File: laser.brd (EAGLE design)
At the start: 7 parts

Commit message: Test layout
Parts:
- removed E$2: (no value), EasyDriver:EASYDRIVER_V44
- added DC_JACK: (no value), SparkFun-Connectors:POWER_JACK_SLOT
- added E$7: (no value), SparkFun-DiscreteSemi:TO-92
- added E$8: (no value), SparkFun-DiscreteSemi:DIODE-1N4001
- added E$9: (no value), eagle-ltspice:0204/7
- added END_X1, END_Y1, FAN, FAN1, LASER: (no value), pinhead:1X02
- added LM317: (no value), v-reg:78XXL
- added X_AXIS, Y_AXIS: (no value), EasyDriver:EASYDRIVER_V44
- added X_AXIS_CON, Y_AXIS_CON: (no value), SparkFun-Connectors:1X04_LONGPADS
- E$1: device v-reg:78XXL -> heatsink:D01S
- E$3: device EasyDriver:EASYDRIVER_V44 -> jumper:0R/10E
- E$5: device SparkFun-Resistors:AXIAL-0.6 -> jumper:07
- NANO: value (none) -> NANO
- moved E$3 76.0 mm to (-6.35, 71.1), turned to 180 degrees
- moved E$1 62.2 mm to (69.8, 52.1)
- moved E$5 48.7 mm to (-6.35, 68.6), turned to 180 degrees
- moved NANO 45.8 mm to (33.0, 74.9)
- moved E$4 44.3 mm to (62.2, 35.6), turned to 180 degrees
- moved E$6 19.1 mm to (66.0, 72.4), turned to 180 degrees
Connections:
- new net 12V: DC_JACK.PWR, E$8.A, FAN.2, FAN1.2, X_AXIS.M+, Y_AXIS.M+
- new net 5V: NANO.D9, X_AXIS.MS1, X_AXIS.MS2, X_AXIS.P$11, Y_AXIS.MS1, Y_AXIS.MS2, Y_AXIS.P$11
- new net GND: DC_JACK.GND@1, DC_JACK.GND@2, E$7.3, END_X1.2, END_Y1.2, FAN.1, FAN1.1, NANO.A7, NANO.D11, X_AXIS.GND1, X_AXIS.GND2, X_AXIS.GND3, Y_AXIS.GND1, Y_AXIS.GND2, Y_AXIS.GND3
- new net S$1: NANO.A6, Y_AXIS.STEP
- new net S$10: X_AXIS.B1, X_AXIS_CON.1
- new net S$11: Y_AXIS.B1, Y_AXIS_CON.1
- new net S$12: Y_AXIS.B2, Y_AXIS_CON.2
- new net S$13: Y_AXIS.A2, Y_AXIS_CON.3
- new net S$14: Y_AXIS.A1, Y_AXIS_CON.4
- new net S$15: E$8.C, LM317.IN
- new net S$16: E$4.P$2, LM317.OUT
- new net S$17: E$4.P$1, E$6.A, E$6.S
- new net S$18: E$6.E, LASER.2, LM317.GND
- new net S$19: E$9.1, NANO.VIN
- new net S$2: NANO.A5, X_AXIS.STEP
- new net S$20: E$7.2, E$9.2
- new net S$21: E$7.1, LASER.1
- new net S$3: NANO.A3, Y_AXIS.DIR
- new net S$4: NANO.A2, X_AXIS.DIR
- new net S$7: X_AXIS.A1, X_AXIS_CON.4
- new net S$8: X_AXIS.A2, X_AXIS_CON.3
- new net S$9: X_AXIS.B2, X_AXIS_CON.2
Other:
- board outline added: 7.1 x 7.3 mm

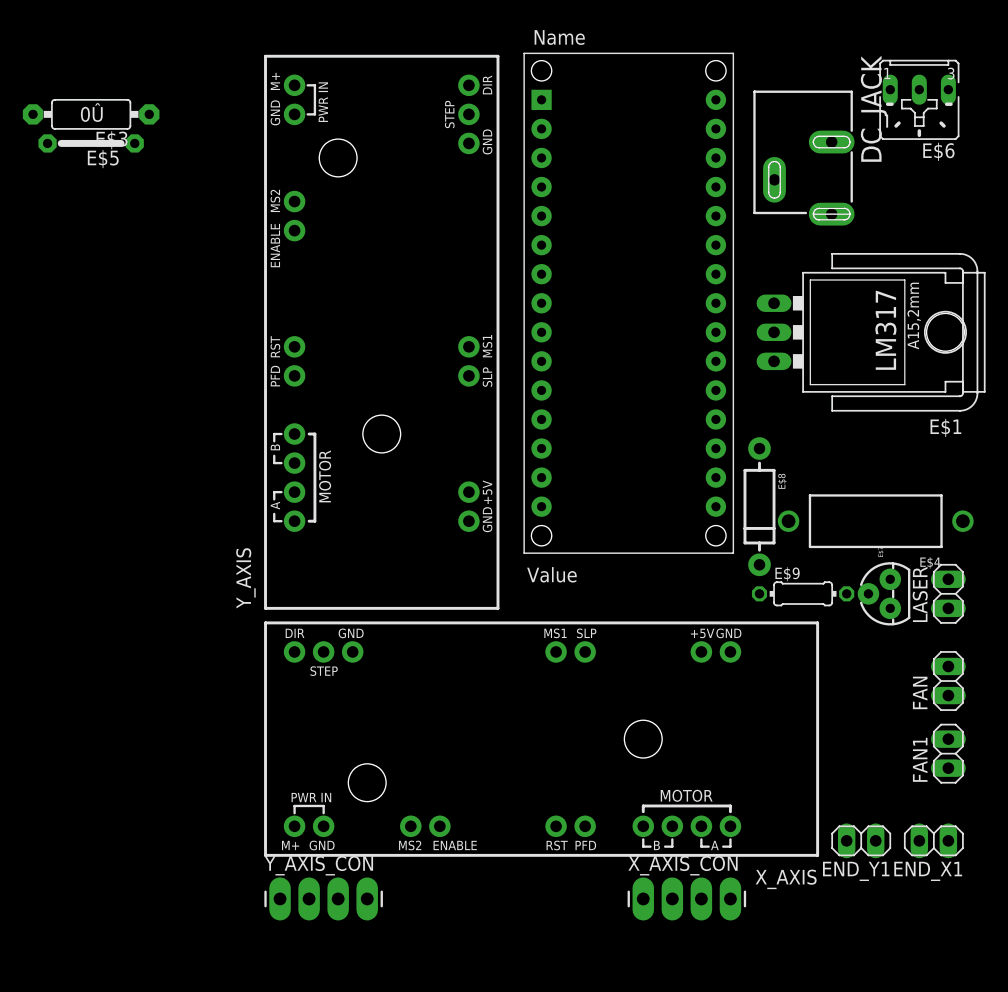
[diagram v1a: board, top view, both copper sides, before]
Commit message: Test layout, added power switch
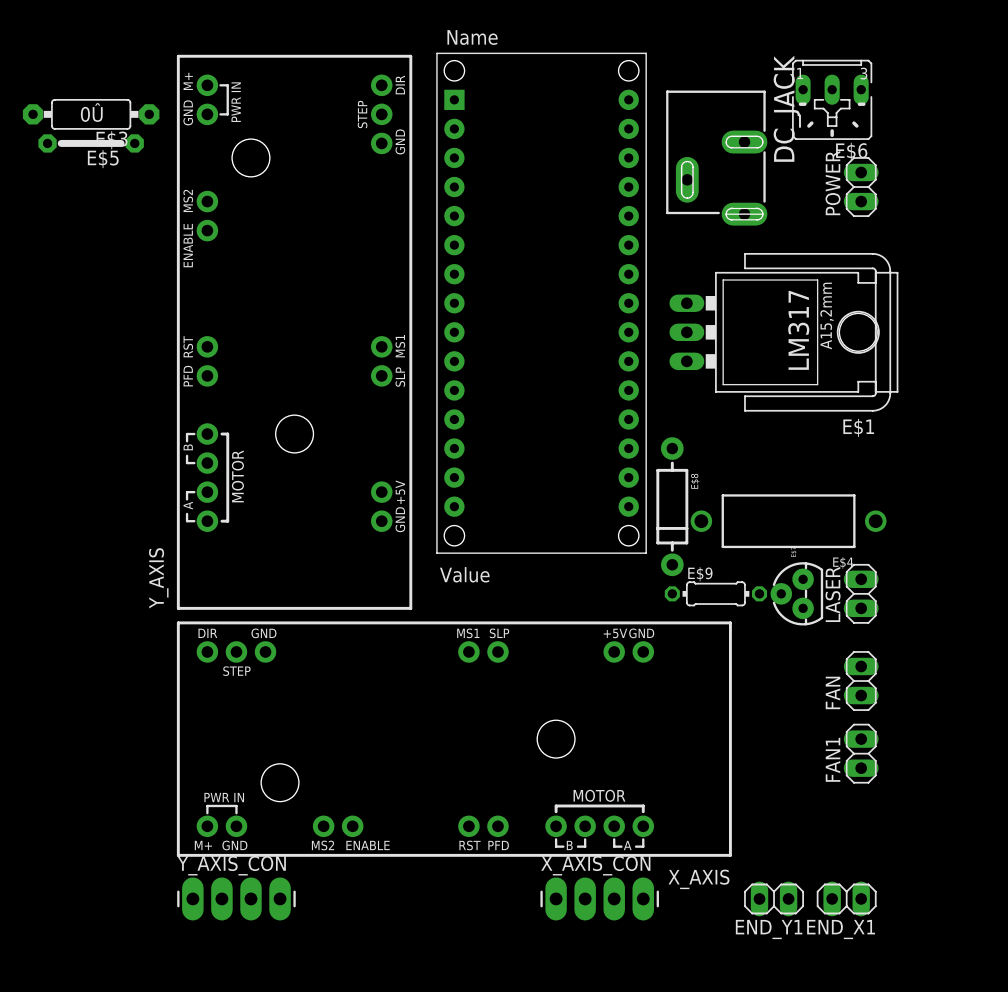
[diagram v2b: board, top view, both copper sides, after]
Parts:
- added POWER: (no value), pinhead:1X02
- moved END_X1 9.16 mm to (59.7, 2.54)
- moved END_Y1 9.16 mm to (53.3, 2.54)
- moved E$6 7.62 mm to (58.4, 72.4)
- moved E$9 7.62 mm to (48.3, 29.2)
- moved NANO 7.62 mm to (25.4, 74.9)
- moved X_AXIS 7.62 mm to (25.4, 16.5)
- moved Y_AXIS 7.62 mm to (11.4, 52.1)
- moved Y_AXIS_CON 7.62 mm to (2.54, 2.54)
- moved DC_JACK 7.62 mm to (53.3, 76.2)
- moved E$1 7.62 mm to (62.2, 52.1)
- moved E$4 7.62 mm to (54.6, 35.6)
- moved E$7 7.62 mm to (55.9, 29.2)
- moved E$8 7.62 mm to (44.5, 36.8)
- moved FAN 7.62 mm to (61.0, 21.6)
- moved FAN1 7.62 mm to (61.0, 15.2)
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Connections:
- net 12V: now also POWER.1, POWER.2
